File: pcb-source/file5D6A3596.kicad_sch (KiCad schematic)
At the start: 21 parts, among them J2 Program_enable, J6 Conn_02x03_Odd_Even, J7 ST-LINK, U2 MAX3232, U5 MCP795xx, U6 STM32C031CxT, Y1 32KHz

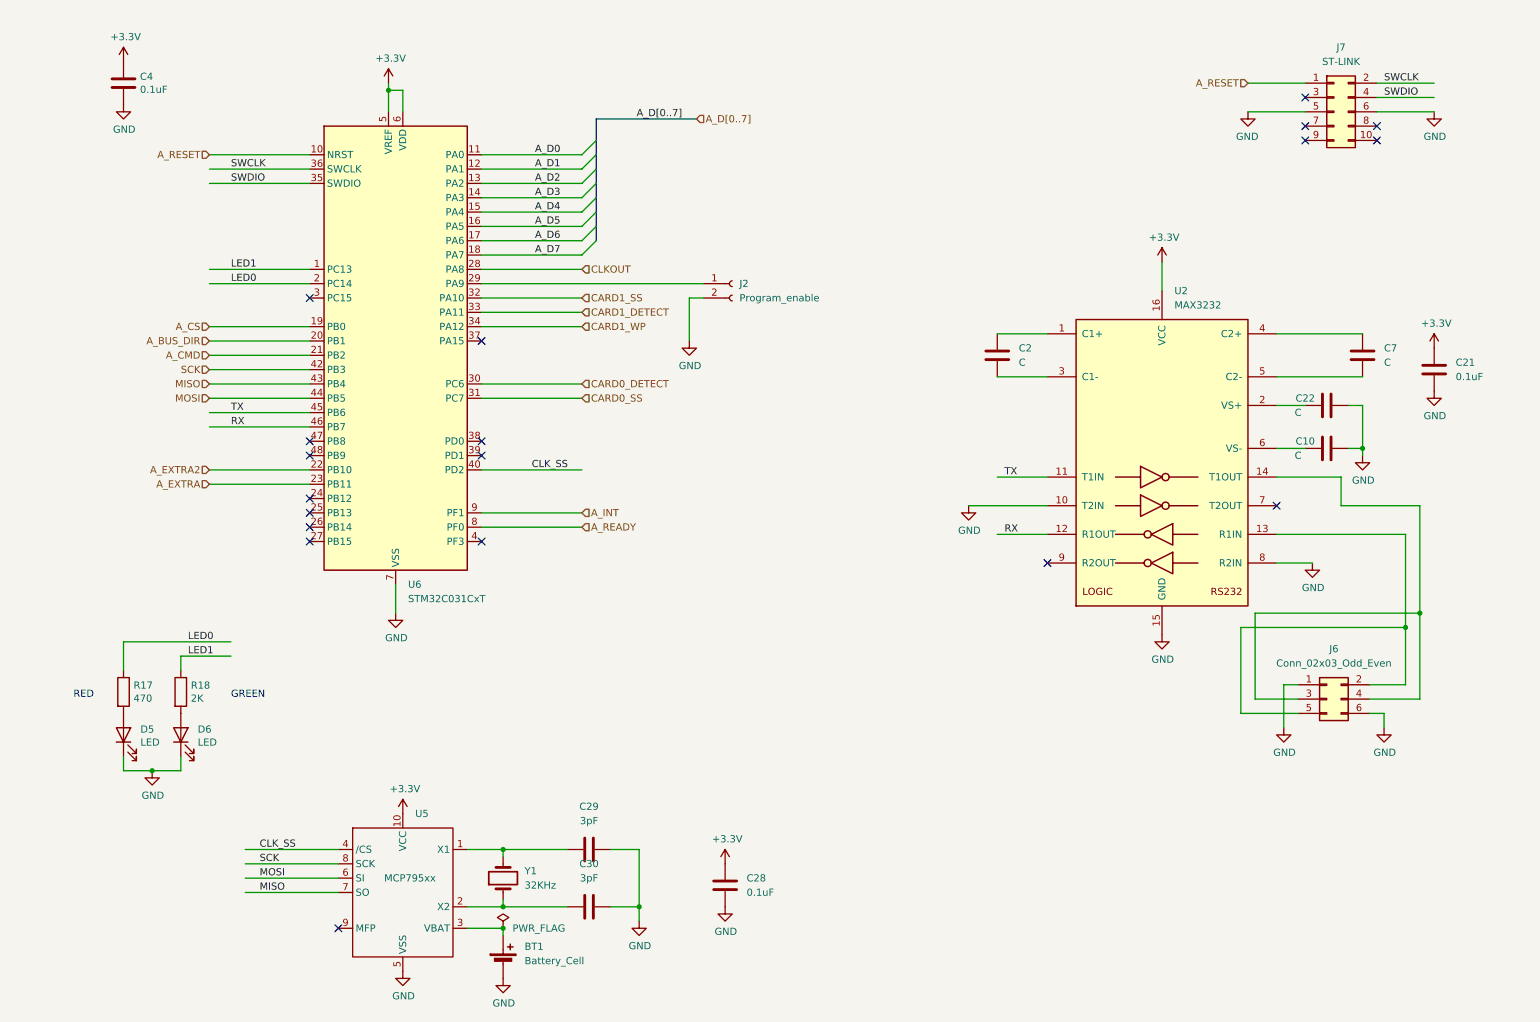
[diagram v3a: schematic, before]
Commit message: 1.2 version with 2 SPI buses
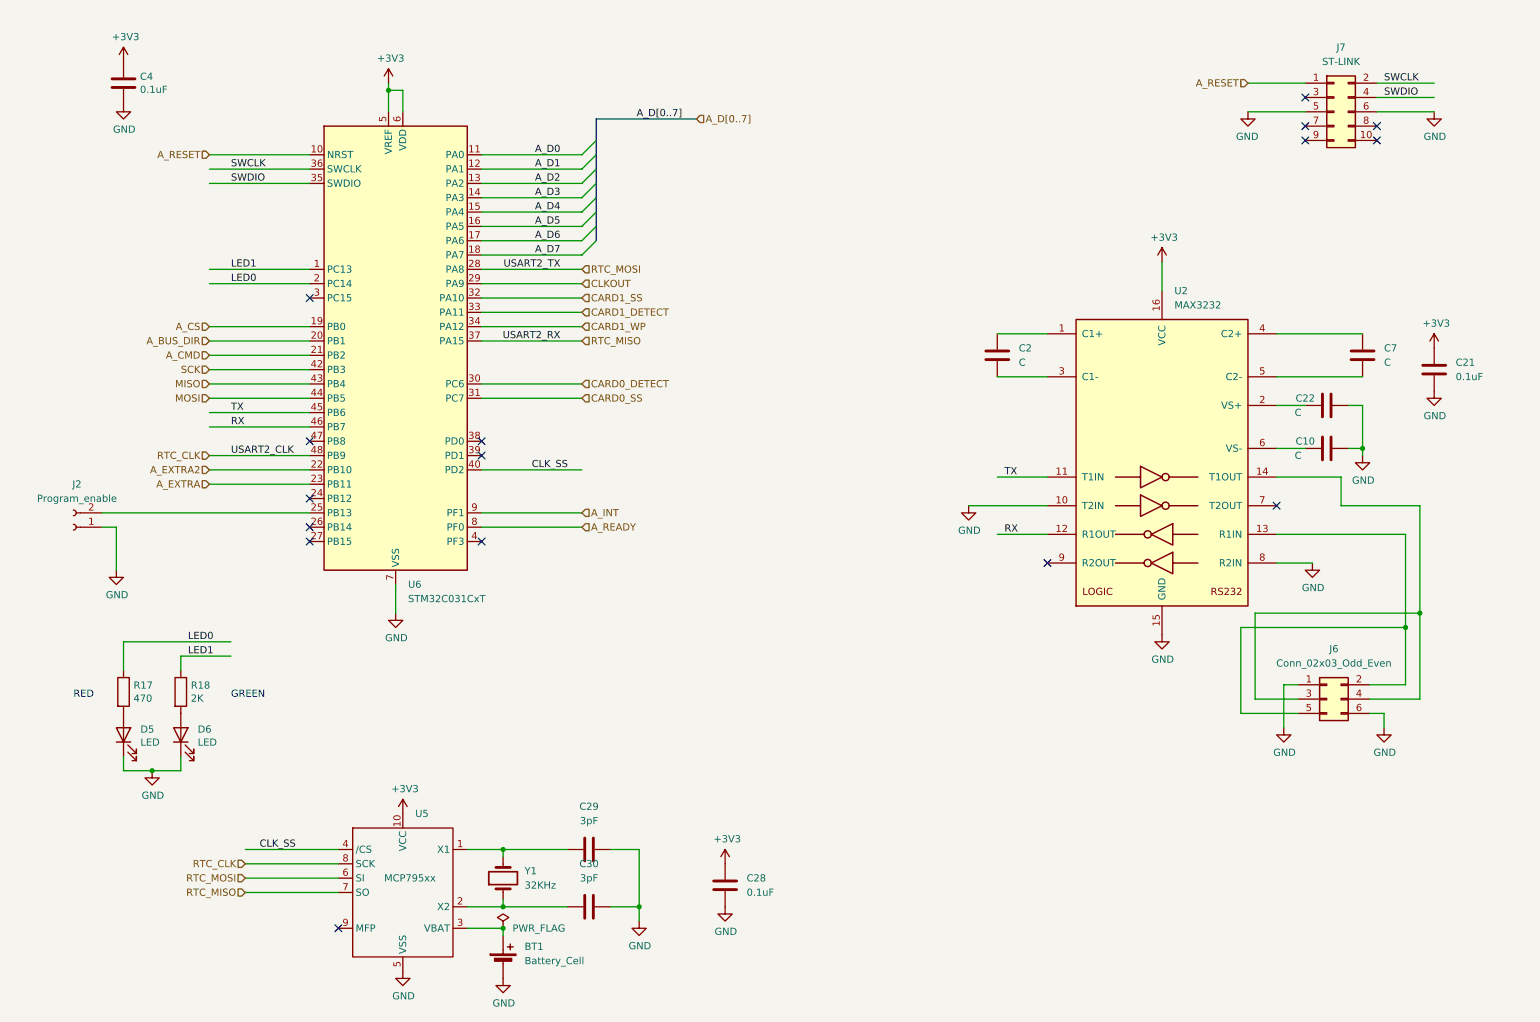
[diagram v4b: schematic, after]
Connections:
- net CLKOUT: now also U6.29 (PA9); no longer U6.28 (PA8)
- net GND: now also J2.1 (Pin_1); no longer J2.2 (Pin_2)
- net MISO: no longer U5.7 (SO)
- net MOSI: no longer U5.6 (SI)
- net SCK: no longer U5.8 (SCK)
- net at U6.25 (PB13): now also J2.2 (Pin_2)
- net RTC_MISO: now reaches U6.37 (PA15)
- net RTC_MISO: now also U5.7 (SO)
- net RTC_CLK: now reaches U6.48 (PB9)
- net RTC_CLK: now also U5.8 (SCK)
- new net RTC_MOSI: U5.6 (SI), U6.28 (PA8)
- no-connect marks 19 -> 16
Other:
- moved on the sheet: J2
